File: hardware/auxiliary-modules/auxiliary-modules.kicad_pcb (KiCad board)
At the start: 2 copper layers, 40.5 x 74.5 mm, 38 parts, among them J1 IDC-10, J2 IDC-10, J3 Conn_01x04, J4 IDC-10, J5 Conn_01x07, U1 CS49E, U2 NTS0102, U3 LM393, U4 NTS0102

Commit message: ready?
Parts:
- renumbered C13 to C10, C14 to C11, C15 to C12, C10 to C13, C11 to C14, C12 to C15, J5 to J2, J2 to J5, L5 to L4, L4 to L5

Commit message: Mouser
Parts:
- removed L1, L2, L3, L4, L5: 2.2u/1A, Inductor_SMD:L_0603_1608Metric
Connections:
- C1 pad 1: Net-(J1-Pin_2) -> TACH_5V
- C10 pad 1: Net-(J4-Pin_4) -> RANGE_3.3V
- C13 pad 1: Net-(J5-Pin_4) -> FLOW_3.3V
- C4 pad 1: Net-(J1-Pin_4) -> TACH_3.3V
- C7 pad 1: Net-(J4-Pin_2) -> RANGE_5V
- J1 pad 2: Net-(J1-Pin_2) -> TACH_5V
- J1 pad 4: Net-(J1-Pin_4) -> TACH_3.3V
- J4 pad 2: Net-(J4-Pin_2) -> RANGE_5V
- J4 pad 4: Net-(J4-Pin_4) -> RANGE_3.3V
- J5 pad 4: Net-(J5-Pin_4) -> FLOW_3.3V

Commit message: fix connector GPS pinout, update AUX pinouts
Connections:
- J4 pad 1: unconnected-(J4-Pin_1-Pad1) -> /TRIG
- J4 pad 3: unconnected-(J4-Pin_3-Pad3) -> /ECHO
- J4 pad 6: Net-(J4-Pin_6) -> unconnected-(J4-Pin_6-Pad6)
- J4 pad 8: Net-(J4-Pin_8) -> unconnected-(J4-Pin_8-Pad8)
- J5 pad 1: FLOW_SCK -> unconnected-(J5-Pin_1-Pad1)
- J5 pad 3: FLOW_MISO -> unconnected-(J5-Pin_3-Pad3)
- J5 pad 7: unconnected-(J5-Pin_7-Pad7) -> FLOW_SCK
- J5 pad 8: FLOW_CS -> FLOW_MISO
- J5 pad 9: unconnected-(J5-Pin_9-Pad9) -> FLOW_CS
- U4 pad 4: Net-(J4-Pin_6) -> /ECHO
- U4 pad 5: Net-(J4-Pin_8) -> /TRIG
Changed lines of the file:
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@@
 	(net 23 "RANGE_ECHO")
 	(net 24 "unconnected-(J4-Pin_5-Pad5)")
-	(net 25 "Net-(J4-Pin_8)")
+	(net 25 "unconnected-(J4-Pin_6-Pad6)")
 	(net 26 "unconnected-(J4-Pin_9-Pad9)")
-	(net 27 "Net-(J4-Pin_6)")
-	(net 28 "unconnected-(J4-Pin_1-Pad1)")
+	(net 27 "unconnected-(J4-Pin_8-Pad8)")
+	(net 28 "/ECHO")
 	(net 29 "unconnected-(J4-Pin_7-Pad7)")
-	(net 30 "unconnected-(J4-Pin_3-Pad3)")
+	(net 30 "/TRIG")
 	(net 31 "Net-(U2-B1)")
 	(net 32 "Net-(U3A-+)")
@@
 	(net 35 "Net-(U1-Pin_3)")
 	(net 36 "unconnected-(J5-Pin_2-Pad2)")
-	(net 37 "unconnected-(J5-Pin_9-Pad9)")
-	(net 38 "unconnected-(J5-Pin_7-Pad7)")
+	(net 37 "unconnected-(J5-Pin_3-Pad3)")
+	(net 38 "unconnected-(J5-Pin_1-Pad1)")
 	(footprint "Capacitor_SMD:C_0603_1608Metric"
 		(layer "F.Cu")
@@
 			(size 1.1 0.4)
 			(layers "F.Cu" "F.Paste" "F.Mask")
-			(net 27 "Net-(J4-Pin_6)")
+			(net 28 "/ECHO")
 			(pinfunction "A2")
 			(pintype "passive")
@@
 			(size 1.1 0.4)
 			(layers "F.Cu" "F.Paste" "F.Mask")
-			(net 25 "Net-(J4-Pin_8)")
+			(net 30 "/TRIG")
 			(pinfunction "A1")
 			(pintype "passive")
@@
 			(layers "*.Cu" "*.Mask")
 			(remove_unused_layers no)
-			(net 19 "FLOW_SCK")
+			(net 38 "unconnected-(J5-Pin_1-Pad1)")
 			(pinfunction "Pin_1")
-			(pintype "passive")
+			(pintype "passive+no_connect")
 		)
 		(pad "2" thru_hole circle
@@
 			(layers "*.Cu" "*.Mask")
 			(remove_unused_layers no)
-			(net 18 "FLOW_MISO")
+			(net 37 "unconnected-(J5-Pin_3-Pad3)")
 			(pinfunction "Pin_3")
-			(pintype "passive")
+			(pintype "passive+no_connect")
 		)
 		(pad "4" thru_hole circle
@@
 			(layers "*.Cu" "*.Mask")
 			(remove_unused_layers no)
-			(net 38 "unconnected-(J5-Pin_7-Pad7)")
+			(net 19 "FLOW_SCK")
 			(pinfunction "Pin_7")
-			(pintype "passive+no_connect")
+			(pintype "passive")
 		)
 		(pad "8" thru_hole circle
@@
 			(layers "*.Cu" "*.Mask")
 			(remove_unused_layers no)
-			(net 17 "FLOW_CS")
+			(net 18 "FLOW_MISO")
 			(pinfunction "Pin_8")
 			(pintype "passive")
@@
 			(layers "*.Cu" "*.Mask")
 			(remove_unused_layers no)
-			(net 37 "unconnected-(J5-Pin_9-Pad9)")
+			(net 17 "FLOW_CS")
 			(pinfunction "Pin_9")
-			(pintype "passive+no_connect")
+			(pintype "passive")
 		)
 		(pad "10" thru_hole circle
@@
 			(layers "*.Cu" "*.Mask")
 			(remove_unused_layers no)
-			(net 28 "unconnected-(J4-Pin_1-Pad1)")
+			(net 30 "/TRIG")
 			(pinfunction "Pin_1")
-			(pintype "passive+no_connect")
+			(pintype "passive")
 		)
 		(pad "2" thru_hole circle
@@
 			(layers "*.Cu" "*.Mask")
 			(remove_unused_layers no)
-			(net 30 "unconnected-(J4-Pin_3-Pad3)")
+			(net 28 "/ECHO")
 			(pinfunction "Pin_3")
-			(pintype "passive+no_connect")
+			(pintype "passive")
 		)
 		(pad "4" thru_hole circle
@@
 			(layers "*.Cu" "*.Mask")
 			(remove_unused_layers no)
-			(net 27 "Net-(J4-Pin_6)")
+			(net 25 "unconnected-(J4-Pin_6-Pad6)")
 			(pinfunction "Pin_6")
-			(pintype "passive")
+			(pintype "passive+no_connect")
 		)
 		(pad "7" thru_hole circle
@@
 			(layers "*.Cu" "*.Mask")
 			(remove_unused_layers no)
-			(net 25 "Net-(J4-Pin_8)")
+			(net 27 "unconnected-(J4-Pin_8-Pad8)")
 			(pinfunction "Pin_8")
-			(pintype "passive")
+			(pintype "passive+no_connect")
 		)
 		(pad "9" thru_hole circle

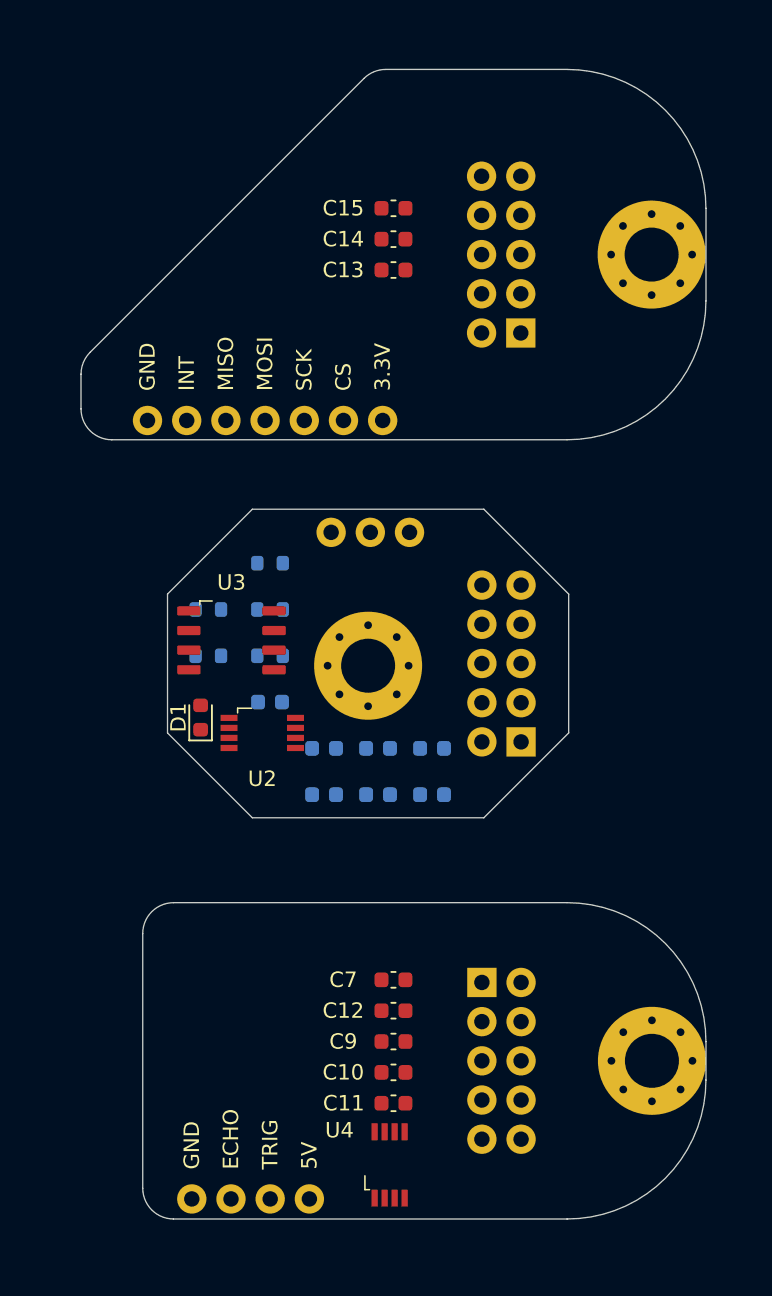
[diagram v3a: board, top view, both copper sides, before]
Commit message: routing: AUX all
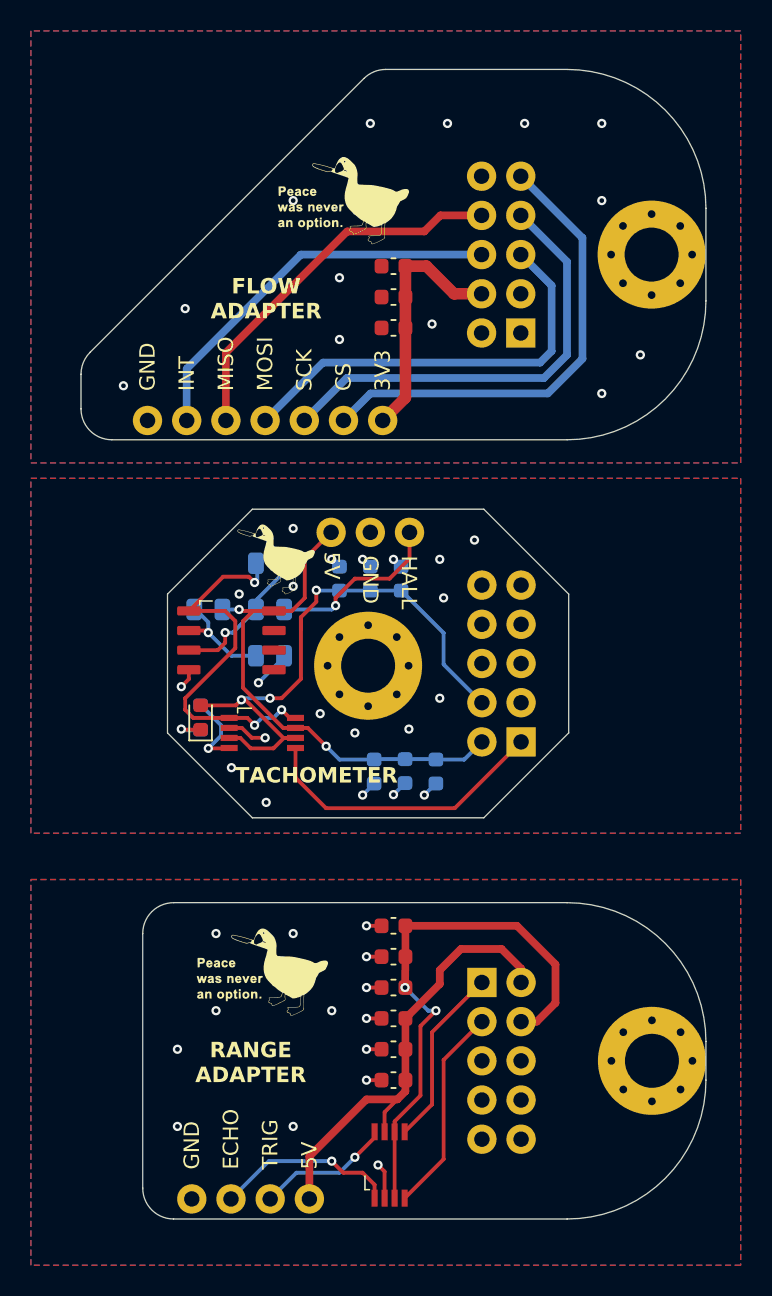
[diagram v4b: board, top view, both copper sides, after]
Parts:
- added G***: LOGO, LOGO, F.Cu at (143.0, 120.0)
- added G***: LOGO, LOGO, F.Cu at (143.0, 93.2)
- added G***: LOGO, LOGO, F.Cu at (148.2, 70.0)
- C8: moved to F.Cu
- R1, R3, R4, R5: footprint Resistor_SMD:R_0603_1608Metric -> Resistor_SMD:R_0805_2012Metric
- moved C8 20.0 mm to (151.5, 125.0)
- moved C5 14.6 mm to (150.0, 94.5), turned to 90 degrees
- moved C6 12.5 mm to (148.0, 94.5), turned to 90 degrees
- moved C1 11.7 mm to (154.2, 107.0), turned to -90 degrees
- moved C4 11.1 mm to (152.0, 94.5), turned to 90 degrees
- moved C10 9.50 mm to (151.5, 117.0), turned to 180 degrees
- moved C11 9.50 mm to (151.5, 119.0), turned to 180 degrees
- moved C15 7.75 mm to (151.5, 78.2), turned to 180 degrees
- moved C2 5.47 mm to (152.2, 107.0), turned to -90 degrees
- moved R2 4.03 mm to (139.0, 103.5), turned to 90 degrees
- moved C14 3.75 mm to (151.5, 76.2), turned to 180 degrees
- moved C7 2.50 mm to (151.5, 123.0), turned to 180 degrees
- moved C9 2.50 mm to (151.5, 127.0), turned to 180 degrees
- moved C3 1.52 mm to (150.2, 107.0), turned to -90 degrees
- moved C12 1.50 mm to (151.5, 121.0), turned to 180 degrees
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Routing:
- net TACH_3.3V: track 0.00 -> 38.5 mm, vias 0 -> 3
- net RANGE_3.3V: track 0.00 -> 35.9 mm, vias 0 -> 2
- net TACH_5V: track 0.00 -> 33.9 mm, vias 0 -> 2
- net FLOW_CS: track 0.00 -> 30.6 mm
- net RANGE_5V: track 0.00 -> 29.2 mm
- net FLOW_SCK: track 0.00 -> 29.1 mm
- net FLOW_MOSI: track 0.00 -> 27.5 mm
- net FLOW_INT: track 0.00 -> 25.5 mm
- net Net-(U2-B1): track 0.00 -> 25.2 mm, vias 0 -> 3
- net FLOW_MISO: track 0.00 -> 24.6 mm
- net TACH: track 0.00 -> 19.1 mm
- net FLOW_3.3V: track 0.00 -> 16.3 mm
- net /ECHO: track 0.00 -> 13.5 mm
- net Net-(U1-Pin_3): track 0.00 -> 11.8 mm, vias 0 -> 1
- net RANGE_ECHO: track 0.00 -> 11.8 mm, vias 0 -> 1
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- added copper zone on B.Cu, net FLOW_GND
- added copper zone on F.Cu, net FLOW_GND
- added copper zone on B.Cu, net RANGE_GND
- added copper zone on F.Cu, net RANGE_GND
- added copper zone on B.Cu, net TACH_GND
- added copper zone on F.Cu, net TACH_GND
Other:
- board text added: "3V3"
- board text added: "BOT"
- board text added: "FB"
- board text added: "FLOW ADAPTER"
- board text added: "HALL"
- board text added: "IN"
- board text added: "RANGE ADAPTER"
- board text added: "TACHOMETER"
- board text added: "TOP"
- board text added: "UAV TVC Goose II Flow Adapter by Eryk Możdżeń August 2024"
- board text added: "UAV TVC Goose II Range Adapter by Eryk Możdżeń August 2024"
- board text added: "UAV TVC Goose II Tachometer by Eryk Możdżeń August 2024"
- board text removed: "3.3V"

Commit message: routing: AUX panelization
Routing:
- net TACH: track 19.1 -> 16.5 mm
- net TACH_GND: vias 21 -> 31
- net RANGE_GND: vias 14 -> 24
- net (no net): vias 0 -> 19
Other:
- outline, holes or cut-outs redrawn
- board text added: "JLCJLCJLCJLC"
